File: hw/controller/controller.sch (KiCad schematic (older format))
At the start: 52 parts, among them J1 ARM-SWD, P1 USB_OTG, P12 UART0, P14 I2C0, P15 I2C1, P16 I2C2, P17 I2C3, P2 FRIDGE, P3 FAN, P4 PUMP, P5 MIST, P6 GND, P7 VDD, SW1 RST, SW2 BOOT, U1 stm32f072x, U2 LDO, U3 tca9546a, Y2 32768Hz

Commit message: Fix merge screwup
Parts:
- removed P1: USB_OTG, footprints:USB_MICRO_B, symbol USB_OTG-RESCUE-controller
- added J2: USB_OTG, footprints:USB_MICRO_B, symbol USB_OTG
- D1, D2, D3: symbol LED-RESCUE-controller -> LED-RESCUE-controller-RESCUE-controller
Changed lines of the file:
@@
 GND
 $Comp
-L LED-RESCUE-controller D3
+L LED-RESCUE-controller-RESCUE-controller D3
 U 1 1 5829AECD
 P 3600 7150
@@
 $EndComp
 $Comp
-L LED-RESCUE-controller D2
+L LED-RESCUE-controller-RESCUE-controller D2
 U 1 1 5829AF4F
 P 3600 6850
@@
 $EndComp
 $Comp
-L LED-RESCUE-controller D1
+L LED-RESCUE-controller-RESCUE-controller D1
 U 1 1 5829AFC5
 P 3600 6550
@@
 MIST
 $Comp
-L USB_OTG-RESCUE-controller P1
-U 1 1 582A896C
-P 6500 6850
-F 0 "P1" H 6825 6725 50  0000 C CNN
-F 1 "USB_OTG" H 6500 7050 50  0000 C CNN
-F 2 "footprints:USB_MICRO_B" V 6450 6750 50  0001 C CNN
-F 3 "" V 6450 6750 50  0000 C CNN
-F 4 "10118192-0001LF" H 6500 6850 60  0001 C CNN "MPN"
-	1    6500 6850
-	-1   0    0    1
-$EndComp
-$Comp
 L GND #PWR014
 U 1 1 582A906E
@@
 	3750 6850 4250 6850
 Wire Wire Line
-	3750 7150 4050 7150
-Wire Wire Line
-	4050 7150 4050 6550
+	4050 7150 3750 7150
+Wire Wire Line
+	4050 6550 4050 7150
 Connection ~ 4050 6850
 Wire Wire Line
@@
 	6400 5000 6050 5000
 Wire Wire Line
-	6200 7050 5650 7050
+	5650 7050 6200 7050
 Wire Wire Line
 	5600 6750 6200 6750
@@
 $EndComp
 Connection ~ 5900 7050
+$Comp
+L USB_OTG J2
+U 1 1 58DB0B16
+P 6500 6850
+F 0 "J2" H 6300 7300 50  0000 L CNN
+F 1 "USB_OTG" H 6300 7200 50  0000 L CNN
+F 2 "footprints:USB_MICRO_B" H 6650 6800 50  0001 C CNN
+F 3 "" H 6650 6800 50  0001 C CNN
+F 4 "10118192-0001LF" H 6500 6850 60  0001 C CNN "MPN"
+	1    6500 6850
+	-1   0    0    1
+$EndComp
 $EndSCHEMATC

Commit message: Adding cheese wedges!
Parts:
- removed P12: UART0, Pin_Headers:Pin_Header_Straight_1x06, symbol CONN_01X06
- removed U2: LDO, footprints:SOT-223, symbol LD1117S33CTR
- added C14, C15, C16, C17, C3: 100nF, Capacitors_SMD:C_0603, symbol C_Small
- added J3: UART, Pin_Headers:Pin_Header_Straight_1x03_Pitch1.27mm, symbol CONN_01X03
- added P1: TH0, Pin_Headers:Pin_Header_Straight_1x04, symbol CONN_01X04
- added P8: TH3, Pin_Headers:Pin_Header_Straight_1x04, symbol CONN_01X04
- added R15, R17, R19, R25: 10k, Resistors_SMD:R_0603, symbol R
- added R16, R18, R20, R26, R27: DNP, Resistors_SMD:R_0603, symbol R
- added U2: MIC550X, footprints:SOT-23(M5), symbol MIC550X
- added U4, U5, U6, U7, U8: SHT3x-DIS, footprints:SHT3x, symbol SHT3x-DIS
- C1, C2, C4, C5, C6, C7, C8, C9: footprint Capacitors_SMD:C_0805 -> Capacitors_SMD:C_0603
- C10: value 100nF -> 1uF; footprint Capacitors_SMD:C_0805 -> Capacitors_SMD:C_0603; MPN CL21B104MBCNNNC -> CL21F105ZAFNNNG
- C11: value 10uF -> 1uF; footprint Capacitors_SMD:C_0805 -> Capacitors_SMD:C_0603; MPN CL21B103KBANNNC -> CL21F105ZAFNNNG
- D1, D2, D3: footprint LEDs:LED_0805 -> LEDs:LED_0603
- P6: value GND -> TH1
- P7: value VDD -> TH2
- R1, R10, R11, R12, R13, R14, R2, R21, R22, R23, R24, R3, R4, R5, R7, R8, R9: footprint Resistors_SMD:R_0805 -> Resistors_SMD:R_0603
- R6: value 1.5k -> DNP; footprint Resistors_SMD:R_0805 -> Resistors_SMD:R_0603; MPN RC0805JR-071K5L -> DNP
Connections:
- net labels added: ADDR_LOCAL, ADDR_TH0, ADDR_TH1, ADDR_TH2, ADDR_TH3, GND_TH0, GND_TH1, GND_TH2, GND_TH3, SCL_TH0, SCL_TH1, SCL_TH2, SCL_TH3, SDA_TH0, SDA_TH1, SDA_TH2, SDA_TH3, VDD_TH0, VDD_TH1, VDD_TH2, VDD_TH3
- wire segments 151 -> 250
- no-connect marks 26 -> 30
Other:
- moved on the sheet: C1, C10, C11, C2, C4, C5, C6, C7, C8, C9, D1, D2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

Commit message: Placement mostly done
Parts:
- removed R27: DNP, Resistors_SMD:R_0603, symbol R
- C6: value 100nF -> 4.7uF; MPN CL21B104MBCNNNC -> CL21A475KQFNNNG
- P1, P14, P15, P16, P17, P6, P7, P8: footprint Pin_Headers:Pin_Header_Straight_1x04 -> Pin_Headers:Pin_Header_Straight_1x04_Pitch2.54mm
- P2, P3, P4, P5: footprint Pin_Headers:Pin_Header_Straight_1x02 -> Pin_Headers:Pin_Header_Straight_1x02_Pitch2.54mm
- R26: value DNP -> 10k
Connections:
- net D_N: now reaches J2.2 (D-), R7.1
- net D_P: now reaches J2.3 (D+), R8.1
- net USB_DM renamed USB_N
- net USB_DP renamed USB_P

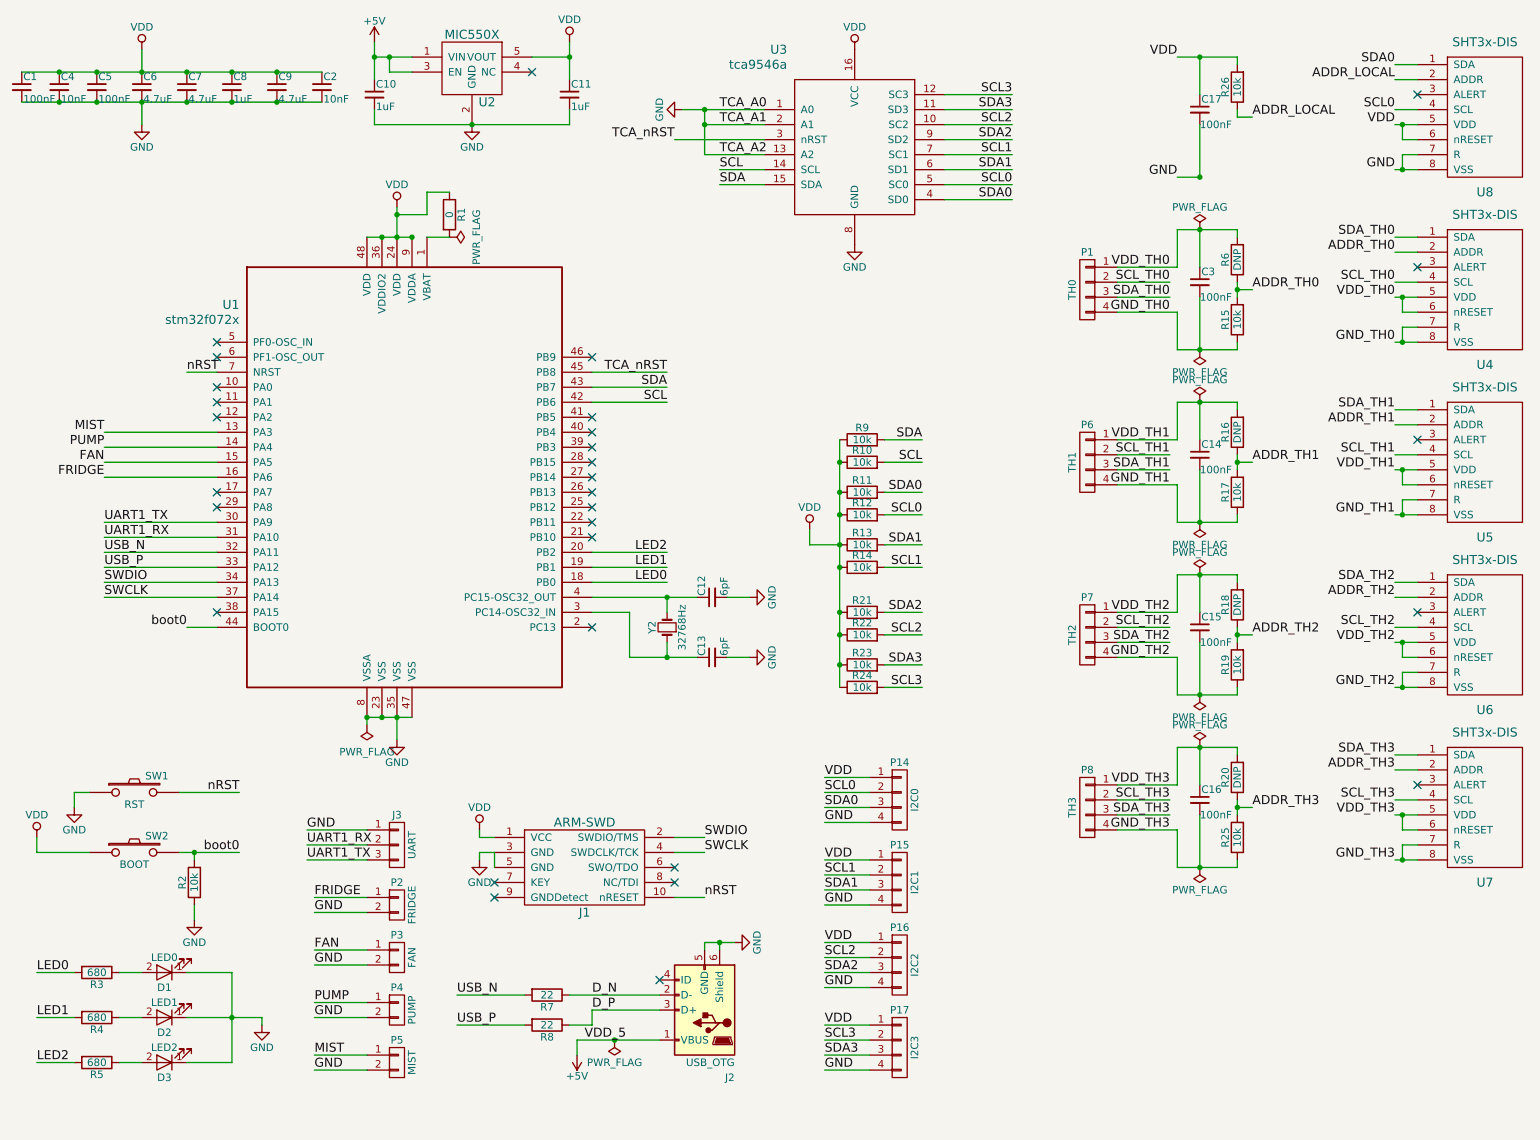
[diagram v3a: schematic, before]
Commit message: Layout done for Ostur Controller v1.3
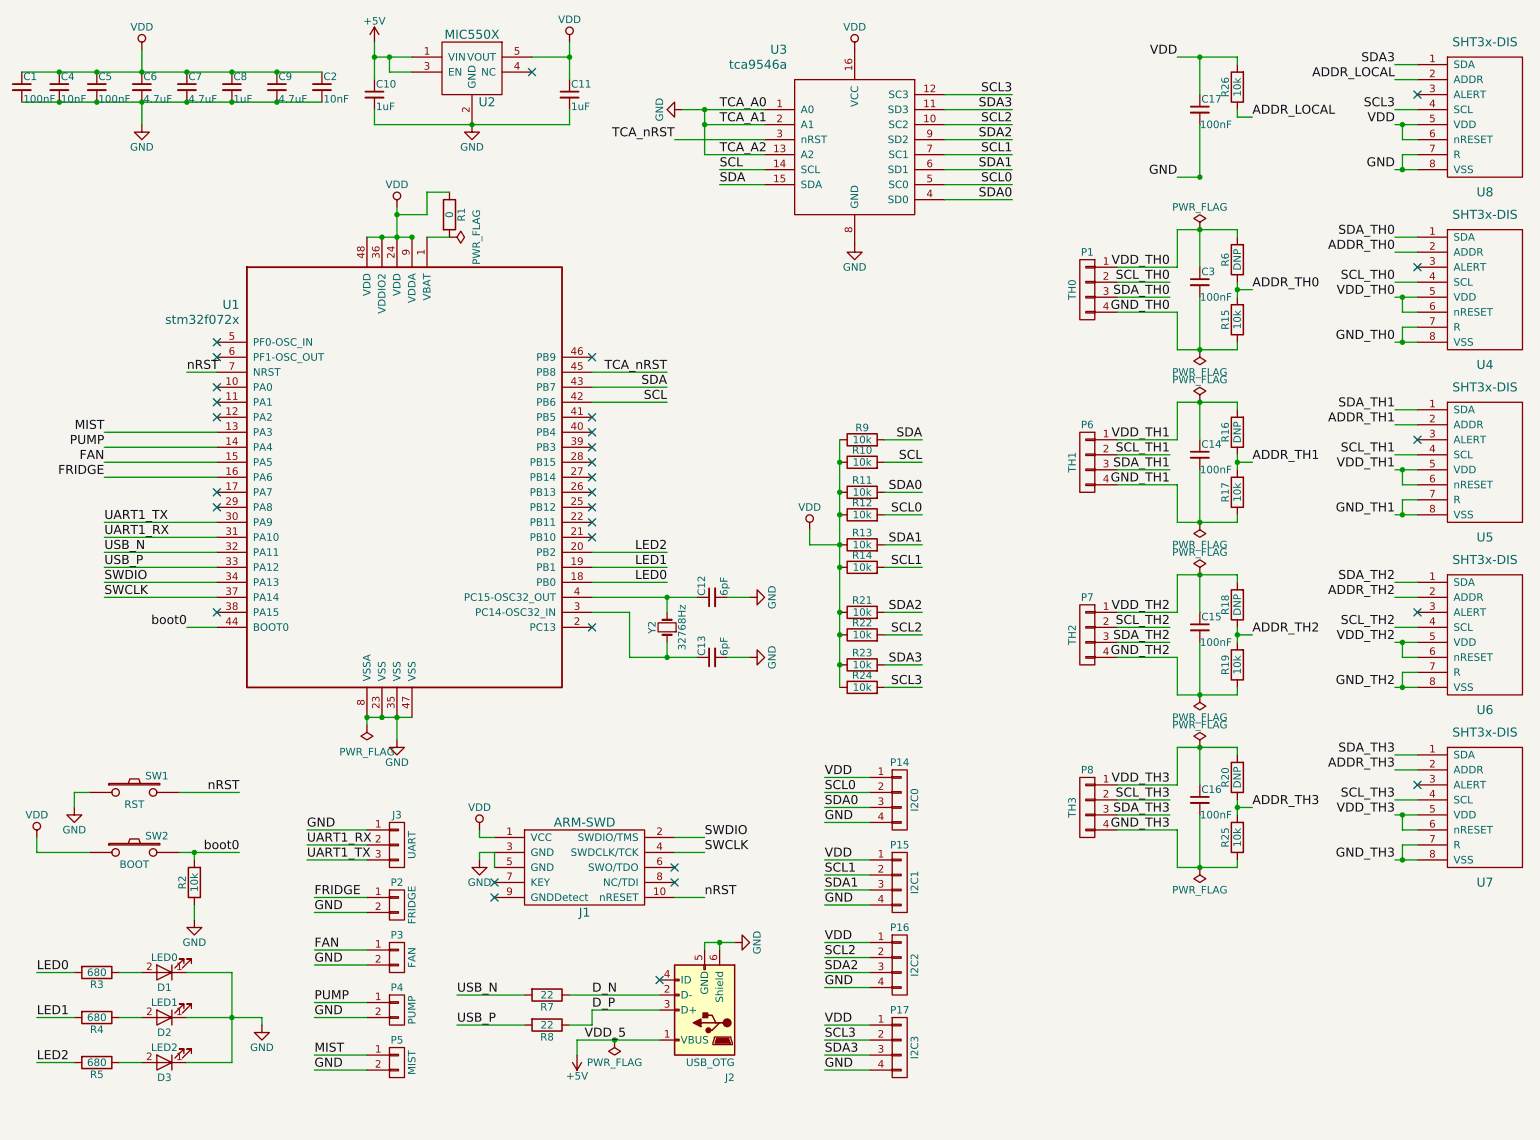
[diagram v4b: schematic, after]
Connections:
- net SCL0: no longer U8.4 (SCL)
- net SCL3: now also U8.4 (SCL)
- net SDA0: no longer U8.1 (SDA)
- net SDA3: now also U8.1 (SDA)
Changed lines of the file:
@@
 	2000 2900 1800 2900
 Wire Wire Line
-	700  900  950  900
-Wire Wire Line
-	950  900  1200 900
-Wire Wire Line
-	1200 900  1500 900
-Wire Wire Line
-	1500 900  1800 900
-Wire Wire Line
-	1800 900  2100 900
-Wire Wire Line
-	2100 900  2400 900
-Wire Wire Line
-	2400 900  2700 900
+	700  900  2700 900
 Connection ~ 1200 900
 Connection ~ 1500 900
 Connection ~ 1800 900
 Wire Wire Line
-	700  1100 950  1100
-Wire Wire Line
-	950  1100 1200 1100
-Wire Wire Line
-	1200 1100 1500 1100
-Wire Wire Line
-	1500 1100 1800 1100
-Wire Wire Line
-	1800 1100 2100 1100
-Wire Wire Line
-	2100 1100 2400 1100
-Wire Wire Line
-	2400 1100 2700 1100
+	700  1100 2700 1100
 Connection ~ 1800 1100
 Connection ~ 1500 1100
@@
 Connection ~ 3300 2000
 Wire Wire Line
-	3200 2000 3200 1850
-Wire Wire Line
-	3200 1850 3200 1800
-Wire Wire Line
-	3000 5200 3100 5200
-Wire Wire Line
-	3100 5200 3200 5200
-Wire Wire Line
-	3200 5200 3300 5200
+	3200 2000 3200 1800
+Wire Wire Line
+	3000 5200 3300 5200
 Connection ~ 3100 5200
 Connection ~ 3200 5200
@@
 	1750 5700 2150 5700
 Wire Wire Line
-	1750 6100 1850 6100
-Wire Wire Line
-	1850 6100 2150 6100
+	1750 6100 2150 6100
 Wire Wire Line
 	800  6100 1150 6100
@@
 	5650 1550 5350 1550
 Wire Wire Line
-	5100 1150 5250 1150
-Wire Wire Line
-	5250 1150 5650 1150
+	5100 1150 5650 1150
 Wire Wire Line
 	5250 1250 5650 1250
@@
 	5250 1450 5650 1450
 Wire Wire Line
-	5250 1150 5250 1250
-Wire Wire Line
-	5250 1250 5250 1450
+	5250 1150 5250 1450
 Connection ~ 5250 1150
 Wire Wire Line
@@
 	1800 6900 2100 6900
 Wire Wire Line
-	1800 7200 2100 7200
-Wire Wire Line
-	2100 7200 2300 7200
+	1800 7200 2300 7200
 Wire Wire Line
 	2100 7500 1800 7500
 Wire Wire Line
-	2100 6900 2100 7200
-Wire Wire Line
-	2100 7200 2100 7500
+	2100 6900 2100 7500
 Connection ~ 2100 7200
 Wire Wire Line
@@
 	2600 6150 3000 6150
 Wire Wire Line
-	4750 4800 5000 4800
-Wire Wire Line
-	5000 4800 5200 4800
-Wire Wire Line
-	4500 4400 5000 4400
-Wire Wire Line
-	5000 4400 5200 4400
+	4750 4800 5200 4800
+Wire Wire Line
+	4500 4400 5200 4400
 Wire Wire Line
 	5000 4700 5000 4800
@@
 	3000 7550 2650 7550
 Wire Wire Line
-	4400 7350 4650 7350
-Wire Wire Line
-	4650 7350 4950 7350
+	4400 7350 4950 7350
 Wire Wire Line
 	4350 7050 4950 7050
@@
 	3600 7250 4050 7250
 Wire Wire Line
-	3050 700  3050 800
-Wire Wire Line
-	3050 800  3050 950
-Wire Wire Line
-	4350 700  4350 800
-Wire Wire Line
-	4350 800  4350 950
-Wire Wire Line
-	3050 1250 3700 1250
-Wire Wire Line
-	3700 1250 4350 1250
+	3050 700  3050 950
+Wire Wire Line
+	4350 700  4350 950
+Wire Wire Line
+	3050 1250 4350 1250
 Wire Wire Line
 	3050 1150 3050 1250
@@
 	6450 3850 6700 3850
 Wire Wire Line
-	6150 3350 6150 3500
-Wire Wire Line
-	6150 3500 6150 3700
-Wire Wire Line
-	6150 3700 6150 3850
-Wire Wire Line
-	6150 3850 6150 4050
-Wire Wire Line
-	6150 4050 6150 4200
-Wire Wire Line
-	6150 4200 6150 4500
-Wire Wire Line
-	6150 4500 6150 4650
-Wire Wire Line
-	6150 4650 6150 4850
-Wire Wire Line
-	6150 4850 6150 5000
+	6150 3350 6150 5000
 Wire Wire Line
 	6450 3350 6700 3350
@@
 SDA0
 Wire Wire Line
-	3000 2000 3100 2000
-Wire Wire Line
-	3100 2000 3200 2000
-Wire Wire Line
-	3200 2000 3300 2000
+	3000 2000 3300 2000
 $Comp
 L R R1
@@
 	5350 6750 5350 6700
 Wire Wire Line
-	5250 6700 5350 6700
-Wire Wire Line
-	5350 6700 5450 6700
+	5250 6700 5450 6700
 Wire Wire Line
 	5250 6750 5250 6700
@@
 	4350 800  4100 800
 Wire Wire Line
-	3050 800  3150 800
-Wire Wire Line
-	3150 800  3300 800
+	3050 800  3300 800
 Wire Wire Line
 	3300 900  3150 900
@@
 $EndComp
 Wire Wire Line
-	8800 2300 8800 2350
-Wire Wire Line
-	8800 2350 8800 2400
+	8800 2300 8800 2400
 Wire Wire Line
 	8800 1950 8800 2000
 Wire Wire Line
-	8400 1950 8550 1950
-Wire Wire Line
-	8550 1950 8800 1950
+	8400 1950 8800 1950
 Wire Wire Line
 	8400 2200 8400 1950
@@
 	8800 2750 8800 2700
 Wire Wire Line
-	8400 2750 8550 2750
-Wire Wire Line
-	8550 2750 8800 2750
+	8400 2750 8800 2750
 Wire Wire Line
 	8550 2200 8550 1950
@@
 	10000 2300 9850 2300
 Wire Wire Line
-	9850 2400 9900 2400
-Wire Wire Line
-	9900 2400 10000 2400
+	9850 2400 10000 2400
 Wire Wire Line
 	10000 2500 9900 2500
@@
 Connection ~ 9900 2400
 Wire Wire Line
-	9850 2700 9900 2700
-Wire Wire Line
-	9900 2700 10000 2700
+	9850 2700 10000 2700
 Wire Wire Line
 	10000 2600 9900 2600
@@
 $EndComp
 Wire Wire Line
-	8800 3450 8800 3500
-Wire Wire Line
-	8800 3500 8800 3550
+	8800 3450 8800 3550
 Wire Wire Line
 	8800 3100 8800 3150
 Wire Wire Line
-	8400 3100 8550 3100
-Wire Wire Line
-	8550 3100 8800 3100
+	8400 3100 8800 3100
 Wire Wire Line
 	8400 3350 8400 3100
@@
 	8800 3900 8800 3850
 Wire Wire Line
-	8400 3900 8550 3900
-Wire Wire Line
-	8550 3900 8800 3900
+	8400 3900 8800 3900
 Wire Wire Line
 	8550 3350 8550 3100
@@
 	10000 3450 9850 3450
 Wire Wire Line
-	9850 3550 9900 3550
-Wire Wire Line
-	9900 3550 10000 3550
+	9850 3550 10000 3550
 Wire Wire Line
 	10000 3650 9900 3650
@@
 Connection ~ 9900 3550
 Wire Wire Line
-	9850 3850 9900 3850
-Wire Wire Line
-	9900 3850 10000 3850
+	9850 3850 10000 3850
 Wire Wire Line
 	10000 3750 9900 3750
@@
 $EndComp
 Wire Wire Line
-	8800 4600 8800 4650
-Wire Wire Line
-	8800 4650 8800 4700
+	8800 4600 8800 4700
 Wire Wire Line
 	8800 4250 8800 4300
 Wire Wire Line
-	8400 4250 8550 4250
-Wire Wire Line
-	8550 4250 8800 4250
+	8400 4250 8800 4250
 Wire Wire Line
 	8400 4500 8400 4250
@@
 	8800 5050 8800 5000
 Wire Wire Line
-	8400 5050 8550 5050
-Wire Wire Line
-	8550 5050 8800 5050
+	8400 5050 8800 5050
 Wire Wire Line
 	8550 4500 8550 4250
@@
 	10000 4600 9850 4600
 Wire Wire Line
-	9850 4700 9900 4700
-Wire Wire Line
-	9900 4700 10000 4700
+	9850 4700 10000 4700
 Wire Wire Line
 	10000 4800 9900 4800
@@
 Connection ~ 9900 4700
 Wire Wire Line
-	9850 5000 9900 5000
-Wire Wire Line
-	9900 5000 10000 5000
+	9850 5000 10000 5000
 Wire Wire Line
 	10000 4900 9900 4900
@@
 $EndComp
 Wire Wire Line
-	8800 5750 8800 5800
-Wire Wire Line
-	8800 5800 8800 5850
+	8800 5750 8800 5850
 Wire Wire Line
 	8800 5400 8800 5450
 Wire Wire Line
-	8400 5400 8550 5400
-Wire Wire Line
-	8550 5400 8800 5400
+	8400 5400 8800 5400
 Wire Wire Line
 	8400 5650 8400 5400
@@
 	8800 6200 8800 6150
 Wire Wire Line
-	8400 6200 8550 6200
-Wire Wire Line
-	8550 6200 8800 6200
+	8400 6200 8800 6200
 Wire Wire Line
 	8550 5650 8550 5400
@@
 	10000 5750 9850 5750
 Wire Wire Line
-	9850 5850 9900 5850
-Wire Wire Line
-	9900 5850 10000 5850
+	9850 5850 10000 5850
 Wire Wire Line
 	10000 5950 9900 5950
@@
 Connection ~ 9900 5850
 Wire Wire Line
-	9850 6150 9900 6150
-Wire Wire Line
-	9900 6150 10000 6150
+	9850 6150 10000 6150
 Wire Wire Line
 	10000 6050 9900 6050
@@
 	8800 800  8800 850
 Wire Wire Line
-	8400 800  8550 800
-Wire Wire Line
-	8550 800  8800 800
+	8400 800  8800 800
 Wire Wire Line
 	8400 1600 8550 1600
@@
 Connection ~ 8550 800
 Wire Wire Line
-	8550 1250 8550 1600
+	8550 1600 8550 1250
 Connection ~ 8550 1600
 Wire Wire Line
@@
 	10000 1150 9850 1150
 Wire Wire Line
-	9850 1250 9900 1250
-Wire Wire Line
-	9900 1250 10000 1250
+	9850 1250 10000 1250
 Wire Wire Line
 	10000 1350 9900 1350
@@
 Connection ~ 9900 1250
 Wire Wire Line
-	9850 1550 9900 1550
-Wire Wire Line
-	9900 1550 10000 1550
+	9850 1550 10000 1550
 Wire Wire Line
 	10000 1450 9900 1450
@@
 VDD
 Text Label 9850 1150 2    60   ~ 0
-SCL0
+SCL3
 Text Label 9850 850  2    60   ~ 0
-SDA0
+SDA3
 Text Label 9850 1550 2    60   ~ 0
 GND
